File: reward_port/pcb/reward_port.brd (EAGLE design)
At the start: 43.2 x 84.7 mm, 16 parts, among them U2 ATTINY2313A

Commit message: more schematic layout
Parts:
- removed S3: SWITCH-MOMENTARY-2SMD-4, SparkFun-Electromechanical:TACTILE_SWITCH_TALL
- added R1: 10K, SparkFun-Resistors:0603-RES
- added RESET: SWITCH-MOMENTARY-2SMD-4, SparkFun-Electromechanical:TACTILE_SWITCH_TALL
- added U$5: 4-POS-DIP, SparkFun-Electromechanical:4-POS-DIP-SMD
- moved U$4 43.8 mm to (-10.2, 15.2)
- moved U$3 4.02 mm to (-1.27, 21.6)
- moved C1 3.59 mm to (-2.54, 27.9)
- moved U$1 3.59 mm to (-0.51, 43.2)
- moved U$2 2.84 mm to (-16.5, 21.6)
- moved SG1 1.27 mm to (-16.6, 9.14)
- moved U2 0.72 mm to (6.60, 9.65)
- moved S2 0.25 mm to (18.2, 42.0)
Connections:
- net +3V6 renamed N$10
- removed net N$5: C1.C, U$3.GND, U$3.GND2
- new net 12V: C1.A, U$2.OUT, U$3.VMOT
- new net DIR: U$3.DIR
- new net N$11: U$3.MS1, U$5.1
- new net N$12: U$3.MS2, U$5.2
- new net N$13: U$3.MS3, U$5.3
- new net N$14: U$1.7, U2.19
- new net N$15: U$1.9, U2.18
- new net N$16: U$1.1, U2.17
- new net STEP: U$3.STEP
- new net VDD33: R1.2, U$1.2, U$2.GND, U$3.VDD, U$5.5, U$5.6, U$5.7, U$5.8, U2.20
- net GND: now also C1.C, RESET.A2, U$1.10, U$1.4, U$1.6, U$1.8, U$2.IN, U$3.GND, U$3.GND2, U2.10
- net N$4: now also R1.1, RESET.B2, U$1.5, U2.1; no longer C1.A, U$3.VMOT
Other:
- board size 43.2 x 84.7 mm -> 43.2 x 64.8 mm

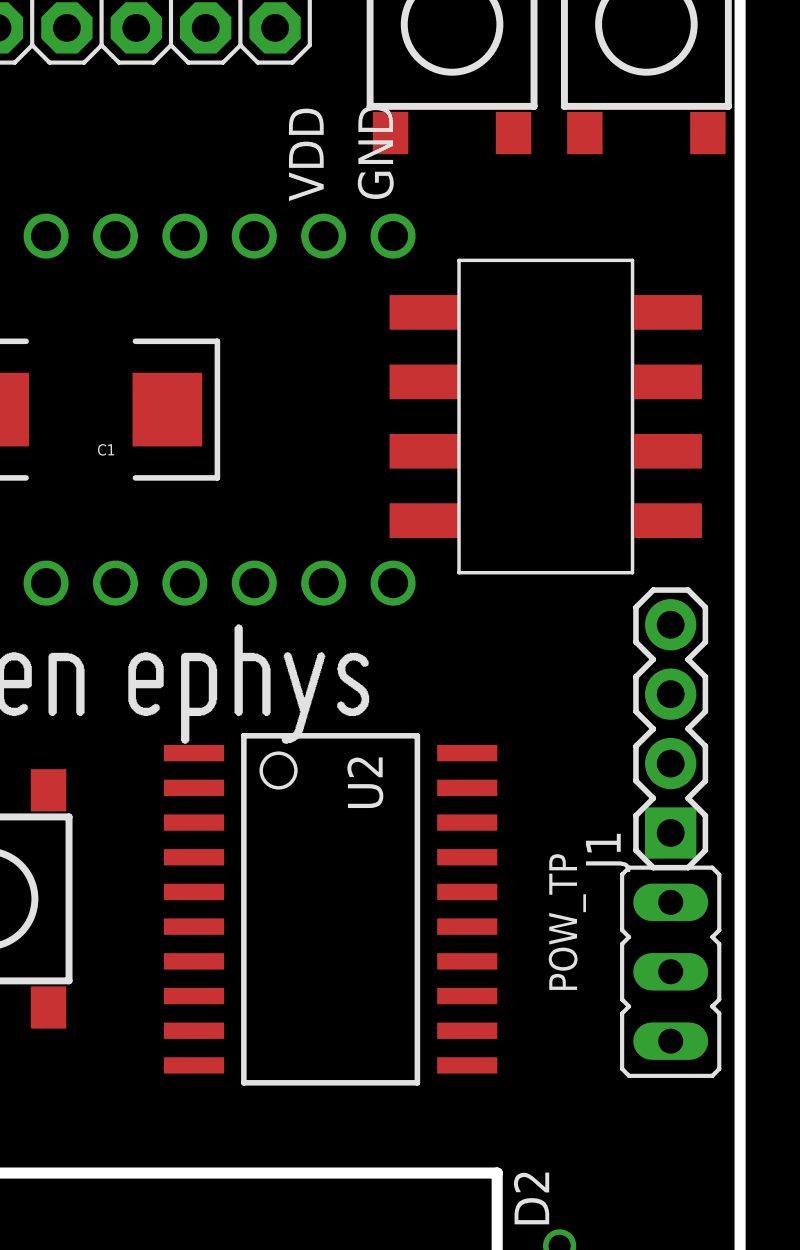
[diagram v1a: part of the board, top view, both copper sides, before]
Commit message: replaced micro controller with attiny84
needed Ain for LED thresholding
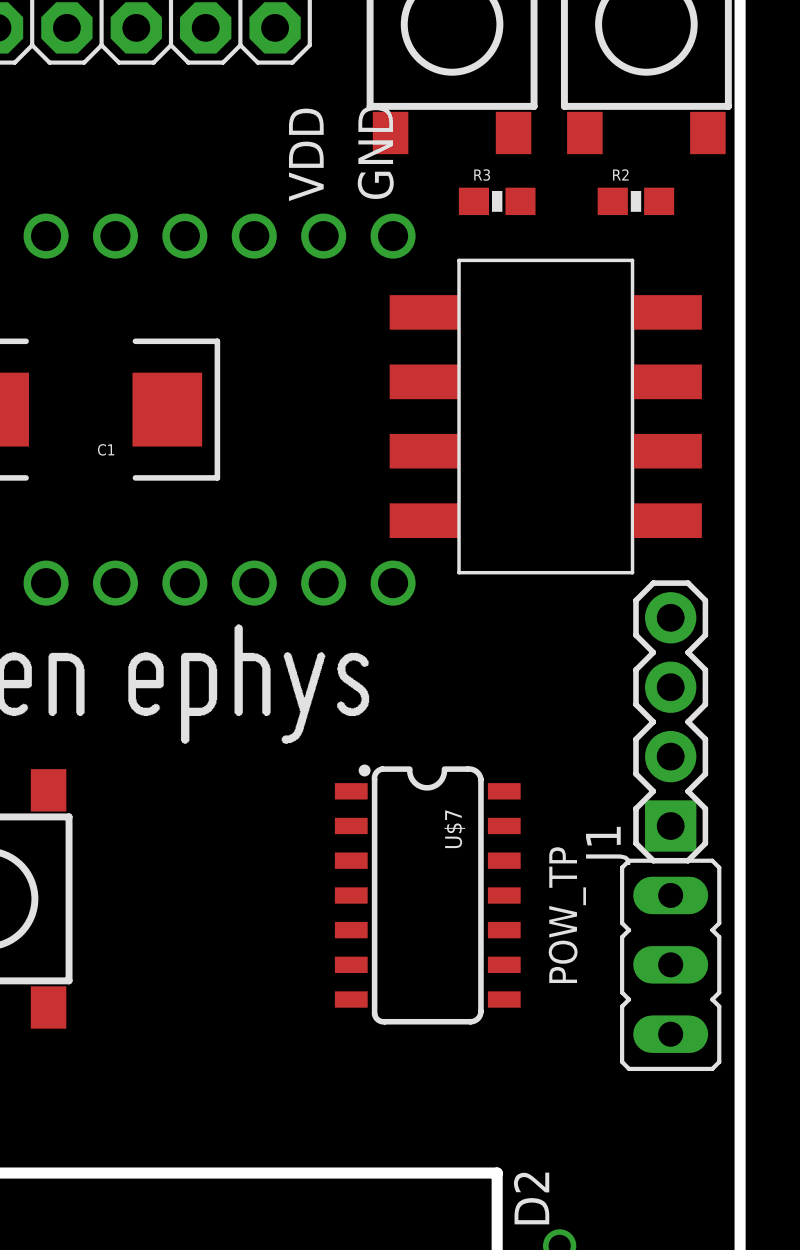
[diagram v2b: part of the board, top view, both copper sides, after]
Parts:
- removed U2: ATTINY2313A, SparkFun-DigitalIC:SOP20W
- added R2, R3: 10K, SparkFun-Resistors:0603-RES
- added U$7: ATTINY84, SparkFun-DigitalIC:SO14
- moved J1 0.25 mm to (19.1, 12.7)
- moved POW_TP 0.25 mm to (19.1, 10.2)
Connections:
- removed net N$15: U$1.9, U2.18
- new net BEEPER: U$7.13
- new net IR_IN: U$7.10
- new net IR_OUT: U$7.11
- new net N$5: U$1.9, U$7.8
- new net STATUS_LED: U$7.12
- new net SW1: R2.2, S2.A2, U$7.2
- new net SW2: R3.2, S1.A2, U$7.6
- net DIR: now also U$7.3
- net GND: now also R2.1, R3.1, U$7.14; no longer U2.10
- net N$14: now also U$7.9; no longer U2.19
- net N$16: now also U$7.7; no longer U2.17
- net N$4: now also U$7.4; no longer U2.1
- net STEP: now also U$7.5
- net VDD33: now also S1.B2, S2.B2, U$7.1; no longer U2.20

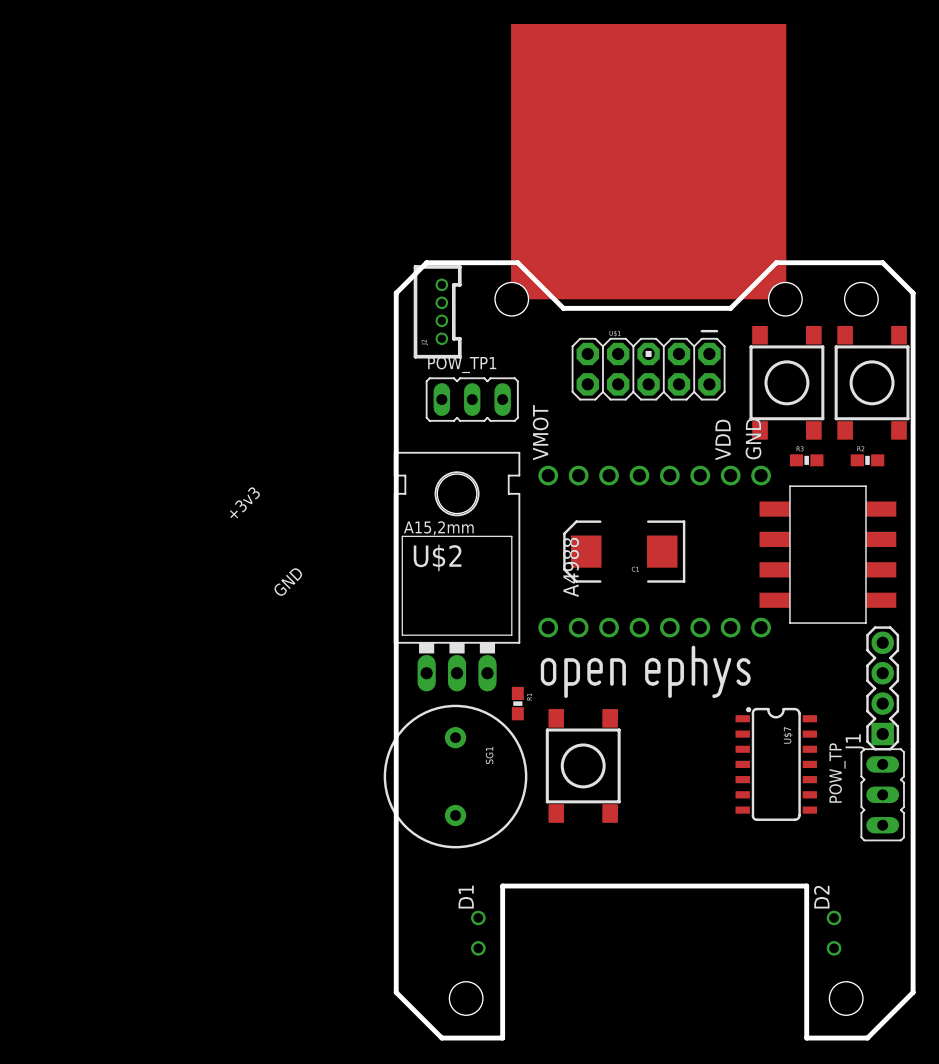
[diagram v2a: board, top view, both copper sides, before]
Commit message: went to atmega32 for i2c bus
at this point the price is getting close to a teensy per port
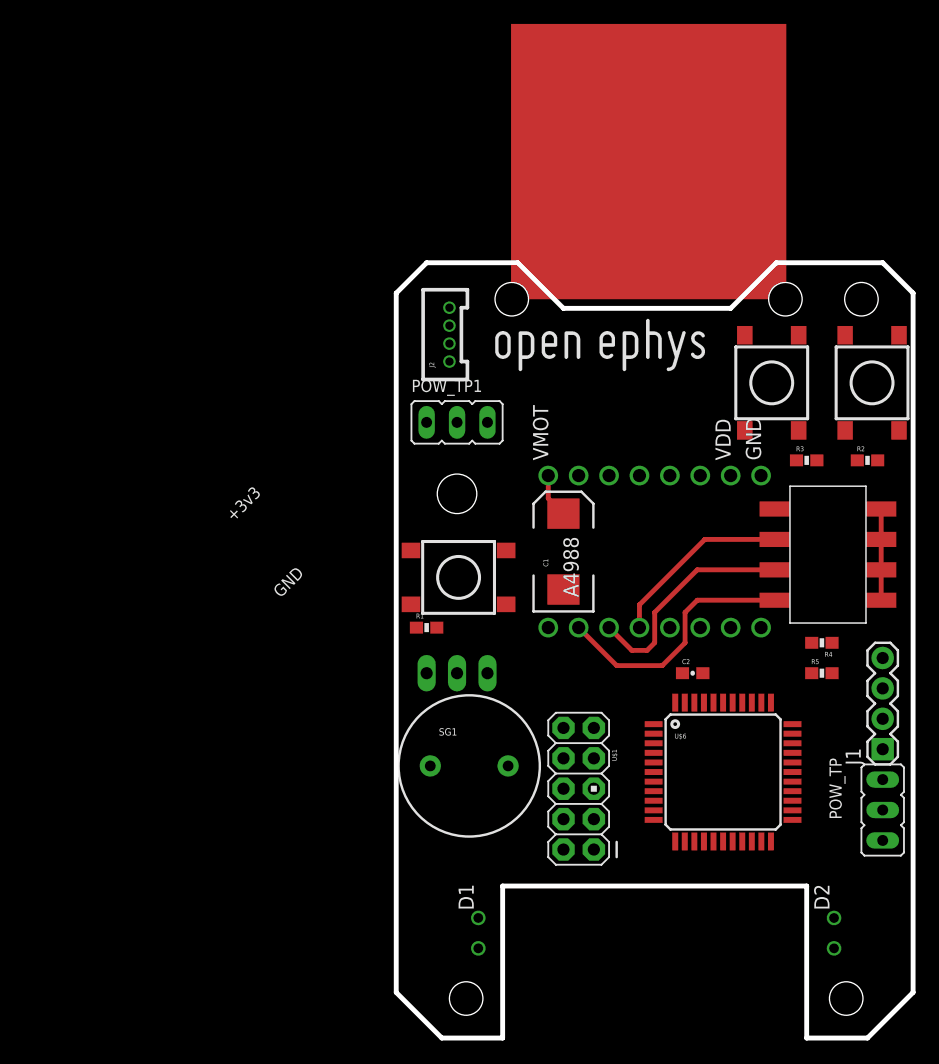
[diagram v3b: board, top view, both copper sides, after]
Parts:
- removed U$7: ATTINY84, SparkFun-DigitalIC:SO14
- added C2: 0.1uF, SparkFun-Capacitors:0603-CAP
- added R4, R5: 10K, SparkFun-Resistors:0603-RES
- added U$6: ATMEGA32U4TQFP-44, SparkFun-DigitalIC:TQFP44
- moved U$1 35.5 mm to (-6.35, 8.13), turned to 180 degrees
- moved U$4 27.6 mm to (-14.0, 42.5)
- moved RESET 18.9 mm to (-16.4, 25.8), turned to 180 degrees
- moved R1 9.92 mm to (-19.1, 21.6), turned to 0 degrees
- moved C1 5.08 mm to (-7.62, 27.9), turned to 90 degrees
- moved POW_TP1 2.29 mm to (-19.1, 38.7)
- moved J2 2.01 mm to (-17.1, 43.8)
- moved SG1 1.45 mm to (-15.5, 10.0), turned to 0 degrees
- moved J1 1.27 mm to (19.1, 11.4)
- moved POW_TP 1.27 mm to (19.1, 8.89)
- moved S1 1.27 mm to (9.78, 42.0)
- flipped U$2 to the bottom
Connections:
- removed net N$10: POW_TP.2
- removed net N$14: U$1.7, U$7.9
- removed net N$16: U$1.1, U$7.7
- removed net N$3: POW_TP.1
- removed net N$4: R1.1, RESET.B2, U$1.5, U$7.4
- removed net N$5: U$1.9, U$7.8
- new net I2C_SCL: J1.4, R4.1, U$6.18
- new net I2C_SDA: J1.3, R5.1, U$6.19
- new net MISO: U$1.9, U$6.11
- new net MOSI: U$1.1, U$6.10
- new net N$15: C2.2, U$6.42
- new net RESET: R1.1, RESET.B2, U$1.5, U$6.13
- new net SCK: U$1.7, U$6.9
- net 12V: now also POW_TP.2
- net BEEPER: now also U$6.41; no longer U$7.13
- net DIR: now also U$6.37; no longer U$7.3
- net GND: now also C2.1, J1.1, POW_TP.1, U$6.15, U$6.23, U$6.35, U$6.43, U$6.5; no longer U$7.14
- net IR_IN: now also U$6.38; no longer U$7.10
- net IR_OUT: now also U$6.39; no longer U$7.11
- net STATUS_LED: now also U$6.40; no longer U$7.12
- net STEP: now also U$6.36; no longer U$7.5
- net SW1: no longer U$7.2
- net SW2: no longer U$7.6
- net VDD33: now also J1.2, R4.2, R5.2, U$6.14, U$6.24, U$6.34, U$6.44; no longer U$7.1
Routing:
- net N$11: track 0.00 -> 21.4 mm
- net N$12: track 0.00 -> 18.9 mm
- net N$13: track 0.00 -> 15.5 mm
- net VDD33: track 0.00 -> 7.73 mm
- net 12V: track 0.00 -> 3.71 mm

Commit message: more layout and sch
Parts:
- removed D1, D2: (no value), SparkFun-LED:LED3MM-NS
- removed J2: (no value), SparkFun-Connectors:1X04-1.5MM_JST
- removed U$4: OPEN_EPHYS_LOGO, open-ephys:OPEN_EPHYS_LOGO
- added C3: 10uF, SparkFun-Capacitors:0603-CAP
- added C4: 0.1uF, SparkFun-Capacitors:0603-CAP
- added DETECTOR, EMITTER: (no value), SparkFun-LED:LED3MM-NS
- added J3: (no value), SparkFun-Connectors:AVR_ICSP
- added J7: (no value), SparkFun-Connectors:MOLEX-1X4
- added R6, R7: 100, SparkFun-Resistors:0603-RES
- moved SG1 35.1 mm to (-1.02, 42.0), turned to 180 degrees
- moved U$1 17.2 mm to (10.8, 9.40)
- moved U$6 5.71 mm to (0.00, 9.53), turned to 45 degrees
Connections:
- removed net VDD33: J1.2, R1.2, R4.2, R5.2, S1.B2, S2.B2, U$1.2, U$2.GND, U$3.VDD, U$5.5, U$5.6, U$5.7, U$5.8, U$6.14, U$6.24, U$6.34, U$6.44
- new net N$20: J3.7, U$6.12
- new net N$21: EMITTER.K, R6.2
- new net N$22: J3.5, U$6.30
- new net N$23: J3.3, U$6.29
- new net N$24: J3.1, U$6.28
- new net N$25: J3.2, U$6.1
- new net N$26: J3.4, U$6.27
- new net N$27: J3.6, U$6.31
- new net N$3: J3.9, U$6.26
- new net VDD: C3.1, J1.2, J3.10, R1.2, R4.2, R5.2, R7.1, S1.B2, S2.B2, U$1.2, U$2.GND, U$3.VDD, U$5.5, U$5.6, U$5.7, U$5.8, U$6.14, U$6.24, U$6.34, U$6.44
- net 12V: now also C4.1
- net BEEPER: now also SG1.-
- net GND: now also C3.2, C4.2, DETECTOR.K, J3.8, R6.1, SG1.+
- net IR_IN: now also DETECTOR.A, R7.2
- net IR_OUT: now also EMITTER.A
- net N$6: now also J7.1; no longer J2.1
- net N$7: now also J7.2; no longer J2.2
- net N$8: now also J7.3; no longer J2.3
- net N$9: now also J7.4; no longer J2.4
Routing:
- net VDD33: track 7.73 -> 0.00 mm
- net VDD: track 0.00 -> 7.73 mm
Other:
- board text added: "detect"
- board text added: "emit"
- board text added: "extension"
- board text added: "programmer"
- board text removed: "GND"
